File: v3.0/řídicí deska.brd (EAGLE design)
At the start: 119 x 37.2 mm, 26 parts, among them IC1 MC78M12ACDTG, IC2 AZ1117CD5, Q1 NX3008, Q2 NX3008, Q3 NX3008

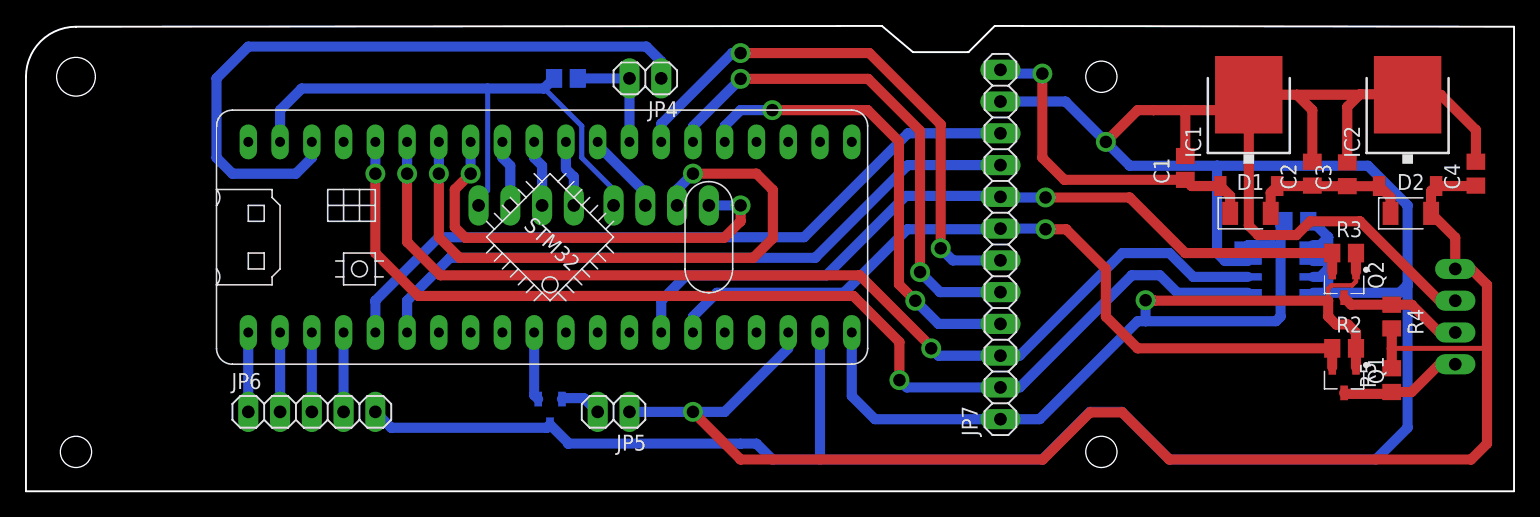
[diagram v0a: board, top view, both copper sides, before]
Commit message: přidána rozlévaná měď, rozšířena dokumentace
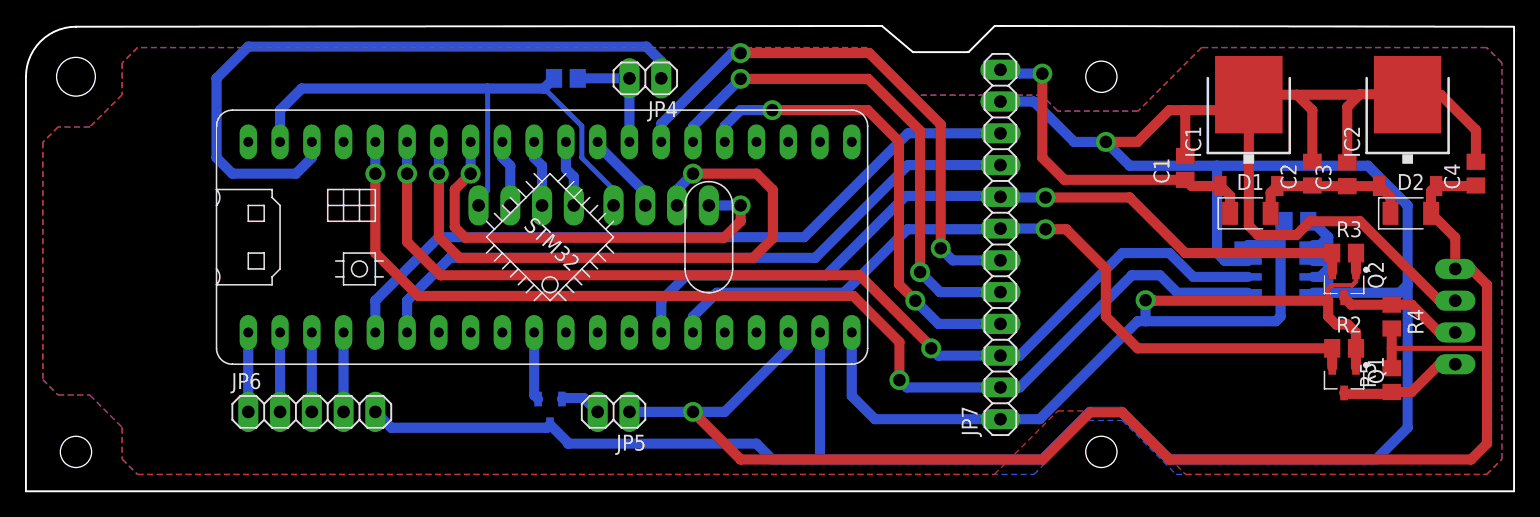
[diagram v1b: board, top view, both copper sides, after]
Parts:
- C1, C2, C3, C4: value 10n -> 100n
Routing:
- added copper zone on layer 1, net GND
- added copper zone on layer 16, net GND
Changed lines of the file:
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@@
 <?xml version="1.0" encoding="utf-8"?>
 <!DOCTYPE eagle SYSTEM "eagle.dtd">
-<eagle version="9.5.1">
+<eagle version="9.7.0">
 <drawing>
 <settings>
@@
 <attribute name="VALUE" x="110.744" y="20.351" size="1.27" layer="27" align="top-center"/>
 </element>
-<element name="C1" library="rcl" library_urn="urn:adsk.eagle:library:334" package="C0805" package3d_urn="urn:adsk.eagle:package:23617/2" value="10n" x="92.71" y="25.8576" smashed="yes" rot="R90">
+<element name="C1" library="rcl" library_urn="urn:adsk.eagle:library:334" package="C0805" package3d_urn="urn:adsk.eagle:package:23617/2" value="100n" x="92.71" y="25.8576" smashed="yes" rot="R90">
 <attribute name="NAME" x="91.44" y="24.5876" size="1.27" layer="25" rot="R90"/>
 <attribute name="POPULARITY" value="88" x="92.71" y="25.8576" size="1.778" layer="27" rot="R90" display="off"/>
@@
 <attribute name="VALUE" x="95.25" y="24.5876" size="1.27" layer="27" rot="R90"/>
 </element>
-<element name="C2" library="rcl" library_urn="urn:adsk.eagle:library:334" package="C0805" package3d_urn="urn:adsk.eagle:package:23617/2" value="10n" x="102.87" y="25.4" smashed="yes" rot="R90">
+<element name="C2" library="rcl" library_urn="urn:adsk.eagle:library:334" package="C0805" package3d_urn="urn:adsk.eagle:package:23617/2" value="100n" x="102.87" y="25.4" smashed="yes" rot="R90">
 <attribute name="NAME" x="101.6" y="24.13" size="1.27" layer="25" rot="R90"/>
 <attribute name="POPULARITY" value="88" x="102.87" y="25.4" size="1.778" layer="27" rot="R90" display="off"/>
@@
 <attribute name="VALUE" x="105.41" y="24.13" size="1.27" layer="27" rot="R90"/>
 </element>
-<element name="C3" library="rcl" library_urn="urn:adsk.eagle:library:334" package="C0805" package3d_urn="urn:adsk.eagle:package:23617/2" value="10n" x="105.664" y="25.3496" smashed="yes" rot="R90">
+<element name="C3" library="rcl" library_urn="urn:adsk.eagle:library:334" package="C0805" package3d_urn="urn:adsk.eagle:package:23617/2" value="100n" x="105.664" y="25.3496" smashed="yes" rot="R90">
 <attribute name="NAME" x="104.394" y="24.0796" size="1.27" layer="25" rot="R90"/>
 <attribute name="POPULARITY" value="88" x="105.664" y="25.3496" size="1.778" layer="27" rot="R90" display="off"/>
@@
 <attribute name="VALUE" x="108.204" y="24.0796" size="1.27" layer="27" rot="R90"/>
 </element>
-<element name="C4" library="rcl" library_urn="urn:adsk.eagle:library:334" package="C0805" package3d_urn="urn:adsk.eagle:package:23617/2" value="10n" x="115.9524" y="25.4" smashed="yes" rot="R90">
+<element name="C4" library="rcl" library_urn="urn:adsk.eagle:library:334" package="C0805" package3d_urn="urn:adsk.eagle:package:23617/2" value="100n" x="115.9524" y="25.4" smashed="yes" rot="R90">
 <attribute name="NAME" x="114.6824" y="24.13" size="1.27" layer="25" rot="R90"/>
 <attribute name="POPULARITY" value="88" x="115.9524" y="25.4" size="1.778" layer="27" rot="R90" display="off"/>
@@
 <wire x1="41.4172" y1="32.2072" x2="42.23" y2="33.02" width="0.8128" layer="16"/>
 <contactref element="Q3" pad="3"/>
-<wire x1="43.35" y1="3.81" x2="57.15" y2="3.81" width="0.8128" layer="16"/>
+<wire x1="43.35" y1="3.81" x2="58.42" y2="3.81" width="0.8128" layer="16"/>
 <wire x1="113.03" y1="15.24" x2="114.3" y2="15.24" width="0.8128" layer="1"/>
 <contactref element="JP6" pad="5"/>
@@
 <wire x1="41.6647" y1="5.08" x2="41.91" y2="5.3253" width="0.8128" layer="16"/>
 <contactref element="JP7" pad="11"/>
-<wire x1="86.36" y1="27.94" x2="83.1342" y2="31.1658" width="0.8128" layer="16"/>
-<wire x1="83.1342" y1="31.1658" x2="77.9282" y2="31.1658" width="0.8128" layer="16"/>
+<wire x1="86.36" y1="27.94" x2="83.82" y2="27.94" width="0.8128" layer="16"/>
+<wire x1="83.82" y1="27.94" x2="80.5942" y2="31.1658" width="0.8128" layer="16"/>
+<wire x1="80.5942" y1="31.1658" x2="77.9282" y2="31.1658" width="0.8128" layer="16"/>
 <via x="86.36" y="27.94" extent="1-16" drill="1"/>
-<wire x1="88.8976" y1="30.4776" x2="90.1676" y2="30.4776" width="0.8128" layer="1"/>
-<wire x1="90.17" y1="30.48" x2="90.1676" y2="30.4776" width="0.8128" layer="1"/>
-<wire x1="90.1676" y1="30.4776" x2="92.71" y2="30.4776" width="0.8128" layer="1"/>
+<wire x1="91.4376" y1="30.4776" x2="92.71" y2="30.4776" width="0.8128" layer="1"/>
 <wire x1="92.71" y1="30.4776" x2="96.5176" y2="30.4776" width="0.8128" layer="1"/>
 <wire x1="96.5176" y1="30.4776" x2="97.79" y2="31.75" width="0.8128" layer="1"/>
@@
 <wire x1="101.64" y1="31.71" x2="106.64" y2="31.71" width="0.8128" layer="1"/>
 <wire x1="106.64" y1="31.71" x2="106.68" y2="31.75" width="0.8128" layer="1"/>
-<wire x1="86.36" y1="27.94" x2="88.8976" y2="30.4776" width="0.8128" layer="1"/>
+<wire x1="91.4376" y1="30.4776" x2="88.9" y2="27.94" width="0.8128" layer="1"/>
+<wire x1="88.9" y1="27.94" x2="86.36" y2="27.94" width="0.8128" layer="1"/>
 <wire x1="102.55" y1="21.59" x2="102.87" y2="21.59" width="0.8128" layer="16"/>
 <wire x1="102.87" y1="21.59" x2="104.14" y2="20.32" width="0.8128" layer="16"/>
@@
 <wire x1="95.885" y1="18.415" x2="95.25" y2="19.05" width="0.8128" layer="16"/>
 <wire x1="95.25" y1="19.05" x2="95.25" y2="26.035" width="0.8128" layer="16"/>
-<wire x1="57.15" y1="3.81" x2="58.42" y2="3.81" width="0.8128" layer="16"/>
 <wire x1="58.42" y1="3.81" x2="59.69" y2="2.54" width="0.8128" layer="16"/>
 <wire x1="59.69" y1="2.54" x2="63.5" y2="2.54" width="0.8128" layer="16"/>
 <wire x1="63.5" y1="12.7" x2="63.5" y2="2.54" width="0.8128" layer="16"/>
-<wire x1="17.78" y1="27.94" x2="20.32" y2="27.94" width="0" layer="19" extent="1-1"/>
-<wire x1="41.91" y1="5.3253" x2="46.99" y2="22.86" width="0" layer="19" extent="16-16"/>
+<polygon width="0.1524" layer="1" spacing="1.27" pour="solid" isolate="0.4064" thermals="yes">
+<vertex x="82.5068375" y="6.4146"/>
+<vertex x="82.53484375" y="6.4262"/>
+<vertex x="87.64515625" y="6.4262"/>
+<vertex x="87.6731625" y="6.4146"/>
+<vertex x="92.7415625" y="1.3462"/>
+<vertex x="116.8084375" y="1.3462"/>
+<vertex x="118.0338" y="2.5715625"/>
+<vertex x="118.0338" y="34.2584375"/>
+<vertex x="116.8084375" y="35.4838"/>
+<vertex x="94.0115625" y="35.4838"/>
+<vertex x="88.9431625" y="30.4154"/>
+<vertex x="88.91515625" y="30.4038"/>
+<vertex x="82.53484375" y="30.4038"/>
+<vertex x="82.5068375" y="30.4154"/>
+<vertex x="81.2484375" y="31.6738"/>
+<vertex x="71.10484375" y="31.6738"/>
+<vertex x="71.0768375" y="31.6854"/>
+<vertex x="67.2784375" y="35.4838"/>
+<vertex x="8.9215625" y="35.4838"/>
+<vertex x="7.6962" y="34.2584375"/>
+<vertex x="7.6962" y="31.73484375"/>
+<vertex x="7.6846" y="31.7068375"/>
+<vertex x="5.1231625" y="29.1454"/>
+<vertex x="5.09515625" y="29.1338"/>
+<vertex x="2.5715625" y="29.1338"/>
+<vertex x="1.3462" y="27.9084375"/>
+<vertex x="1.3462" y="8.9215625"/>
+<vertex x="2.5715625" y="7.6962"/>
+<vertex x="5.09515625" y="7.6962"/>
+<vertex x="5.1231625" y="7.6846"/>
+<vertex x="7.6846" y="5.1231625"/>
+<vertex x="7.6962" y="5.09515625"/>
+<vertex x="7.6962" y="2.5715625"/>
+<vertex x="8.9215625" y="1.3462"/>
+<vertex x="77.4384375" y="1.3462"/>
+</polygon>
+<polygon width="0.1524" layer="16" spacing="1.27" pour="solid" isolate="0.4064" thermals="yes">
+<vertex x="84.9198375" y="5.6526"/>
+<vertex x="84.94784375" y="5.6642"/>
+<vertex x="87.64515625" y="5.6642"/>
+<vertex x="87.6731625" y="5.6526"/>
+<vertex x="91.9795625" y="1.3462"/>
+<vertex x="116.8084375" y="1.3462"/>
+<vertex x="118.0338" y="2.5715625"/>
+<vertex x="118.0338" y="34.2584375"/>
+<vertex x="116.8084375" y="35.4838"/>
+<vertex x="94.0115625" y="35.4838"/>
+<vertex x="88.9431625" y="30.4154"/>
+<vertex x="88.91515625" y="30.4038"/>
+<vertex x="82.53484375" y="30.4038"/>
+<vertex x="82.5068375" y="30.4154"/>
+<vertex x="81.2484375" y="31.6738"/>
+<vertex x="71.10484375" y="31.6738"/>
+<vertex x="71.0768375" y="31.6854"/>
+<vertex x="67.2784375" y="35.4838"/>
+<vertex x="8.9215625" y="35.4838"/>
+<vertex x="7.6962" y="34.2584375"/>
+<vertex x="7.6962" y="31.73484375"/>
+<vertex x="7.6846" y="31.7068375"/>
+<vertex x="5.1231625" y="29.1454"/>
+<vertex x="5.09515625" y="29.1338"/>
+<vertex x="2.5715625" y="29.1338"/>
+<vertex x="1.3462" y="27.9084375"/>
+<vertex x="1.3462" y="8.9215625"/>
+<vertex x="2.5715625" y="7.6962"/>
+<vertex x="5.09515625" y="7.6962"/>
+<vertex x="5.1231625" y="7.6846"/>
+<vertex x="7.6846" y="5.1231625"/>
+<vertex x="7.6962" y="5.09515625"/>
+<vertex x="7.6962" y="2.5715625"/>
+<vertex x="8.9215625" y="1.3462"/>
+<vertex x="80.6134375" y="1.3462"/>
+</polygon>
 </signal>
 <signal name="+3V3">

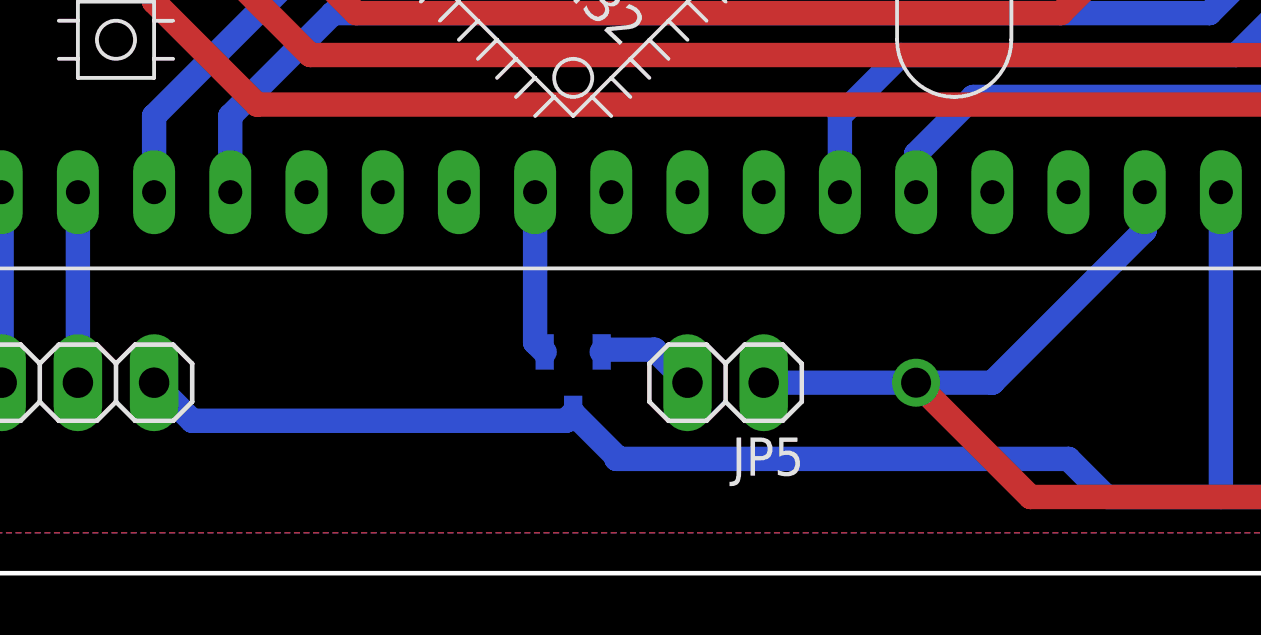
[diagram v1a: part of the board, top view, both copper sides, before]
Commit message: oprava mosfet ventilátoru
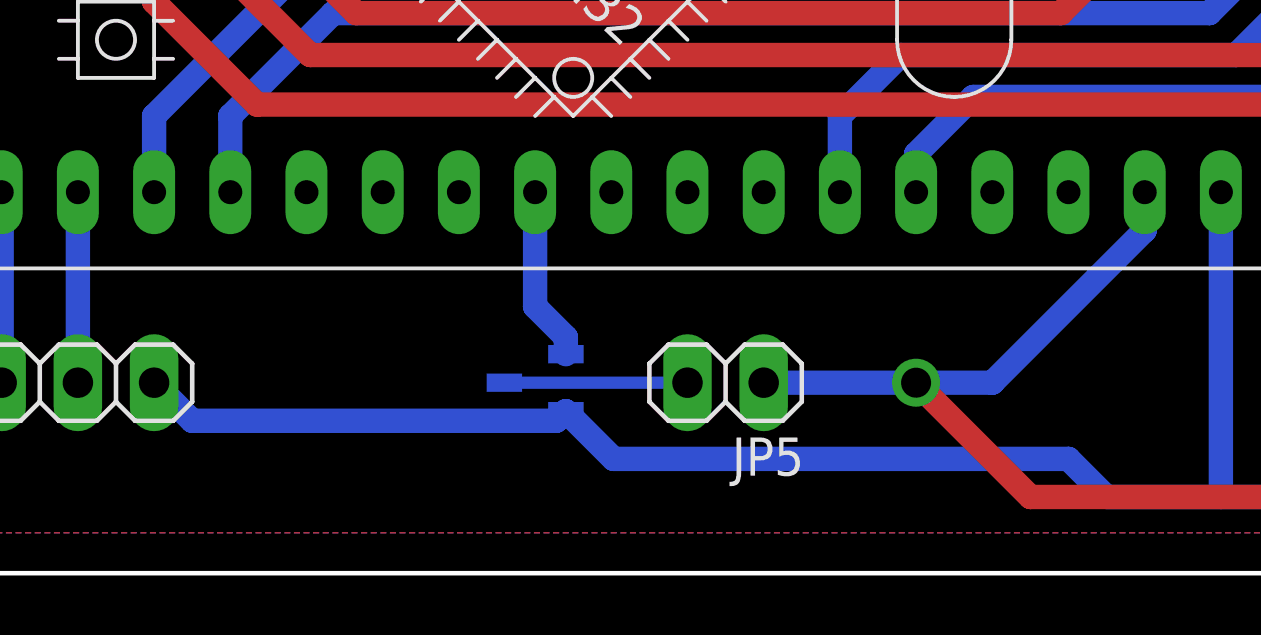
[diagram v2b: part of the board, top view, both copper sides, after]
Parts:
- moved Q3 1.27 mm to (40.6, 6.35), turned to 0 degrees
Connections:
- net GND: now also Q3.2; no longer Q3.3
- net N$5: now also Q3.3; no longer Q3.2
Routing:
- net N$5: track 3.35 -> 6.10 mm
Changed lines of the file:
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@@
 <?xml version="1.0" encoding="utf-8"?>
 <!DOCTYPE eagle SYSTEM "eagle.dtd">
-<eagle version="9.7.0">
+<eagle version="9.5.1">
 <drawing>
 <settings>
@@
 <attribute name="VALUE" x="52.07" y="36.195" size="1.27" layer="27" rot="R180"/>
 </element>
-<element name="Q3" library="NEXPERIA" library_urn="urn:adsk.wipprod:fs.file:vf.nSOLjnv0RT-tOKrwxN9ipw" package="SOT95P240X110-3N" value="NX3008" x="41.91" y="6.35" smashed="yes" rot="MR270">
-<attribute name="NAME" x="40.005" y="8.255" size="1.27" layer="26" rot="MR270"/>
-<attribute name="VALUE" x="45.085" y="8.255" size="1.27" layer="28" rot="MR270"/>
+<element name="Q3" library="NEXPERIA" library_urn="urn:adsk.wipprod:fs.file:vf.nSOLjnv0RT-tOKrwxN9ipw" package="SOT95P240X110-3N" value="NX3008" x="40.64" y="6.35" smashed="yes" rot="MR0">
+<attribute name="NAME" x="42.545" y="8.255" size="1.27" layer="26" rot="MR0"/>
+<attribute name="VALUE" x="42.545" y="3.175" size="1.27" layer="28" rot="MR0"/>
 </element>
 <element name="JP5" library="Connector" package="1X02" package3d_urn="urn:adsk.eagle:package:22435/2" value="PINHD-1X2" x="46.99" y="6.35" smashed="yes" rot="R180">
@@
 <wire x1="36.9196" y1="32.2072" x2="22.0472" y2="32.2072" width="0.8128" layer="16"/>
 <wire x1="41.4172" y1="32.2072" x2="42.23" y2="33.02" width="0.8128" layer="16"/>
-<contactref element="Q3" pad="3"/>
-<wire x1="43.35" y1="3.81" x2="58.42" y2="3.81" width="0.8128" layer="16"/>
 <wire x1="113.03" y1="15.24" x2="114.3" y2="15.24" width="0.8128" layer="1"/>
 <contactref element="JP6" pad="5"/>
 <wire x1="27.94" y1="6.35" x2="29.21" y2="5.08" width="0.8128" layer="16"/>
 <wire x1="97.8388" y1="31.6612" x2="97.79" y2="31.71" width="0.8128" layer="1"/>
-<wire x1="41.91" y1="5.3253" x2="43.35" y2="3.8853" width="0.8128" layer="16"/>
-<wire x1="43.35" y1="3.8853" x2="43.35" y2="3.81" width="0.8128" layer="16"/>
-<wire x1="29.21" y1="5.08" x2="41.6647" y2="5.08" width="0.8128" layer="16"/>
-<wire x1="41.6647" y1="5.08" x2="41.91" y2="5.3253" width="0.8128" layer="16"/>
 <contactref element="JP7" pad="11"/>
 <wire x1="86.36" y1="27.94" x2="83.82" y2="27.94" width="0.8128" layer="16"/>
@@
 <wire x1="59.69" y1="2.54" x2="63.5" y2="2.54" width="0.8128" layer="16"/>
 <wire x1="63.5" y1="12.7" x2="63.5" y2="2.54" width="0.8128" layer="16"/>
-<polygon width="0.1524" layer="1" spacing="1.27" pour="solid" isolate="0.4064" thermals="yes">
+<polygon width="0.1524" layer="1" isolate="0.4064">
 <vertex x="82.5068375" y="6.4146"/>
 <vertex x="82.53484375" y="6.4262"/>
@@
 <vertex x="77.4384375" y="1.3462"/>
 </polygon>
-<polygon width="0.1524" layer="16" spacing="1.27" pour="solid" isolate="0.4064" thermals="yes">
+<polygon width="0.1524" layer="16" isolate="0.4064">
 <vertex x="84.9198375" y="5.6526"/>
 <vertex x="84.94784375" y="5.6642"/>
@@
 <vertex x="80.6134375" y="1.3462"/>
 </polygon>
+<contactref element="Q3" pad="2"/>
+<wire x1="29.21" y1="5.08" x2="41.3447" y2="5.08" width="0.8128" layer="16"/>
+<wire x1="41.3447" y1="5.08" x2="41.6647" y2="5.4" width="0.8128" layer="16"/>
+<wire x1="41.6647" y1="5.4" x2="43.2547" y2="3.81" width="0.8128" layer="16"/>
+<wire x1="43.2547" y1="3.81" x2="58.42" y2="3.81" width="0.8128" layer="16"/>
+<wire x1="17.78" y1="27.94" x2="20.32" y2="27.94" width="0" layer="19" extent="1-1"/>
+<wire x1="41.6647" y1="5.4" x2="46.99" y2="22.86" width="0" layer="19" extent="16-16"/>
 </signal>
 <signal name="+3V3">
@@
 <signal name="PA15">
 <contactref element="U$1" pad="P$10"/>
-<wire x1="40.64" y1="12.7" x2="40.64" y2="7.6947" width="0.8128" layer="16"/>
 <contactref element="Q3" pad="1"/>
-<wire x1="40.64" y1="7.6947" x2="40.96" y2="7.3747" width="0.8128" layer="16"/>
+<wire x1="41.6647" y1="7.3" x2="41.6647" y2="7.8653" width="0.8128" layer="16"/>
+<wire x1="41.6647" y1="7.8653" x2="40.64" y2="8.89" width="0.8128" layer="16"/>
+<wire x1="40.64" y1="8.89" x2="40.64" y2="12.7" width="0.8128" layer="16"/>
 </signal>
 <signal name="N$5">
-<contactref element="Q3" pad="2"/>
 <contactref element="JP5" pad="2"/>
-<wire x1="45.72" y1="6.35" x2="44.62" y2="7.45" width="0.8128" layer="16"/>
-<wire x1="44.62" y1="7.45" x2="42.9353" y2="7.45" width="0.8128" layer="16"/>
-<wire x1="42.9353" y1="7.45" x2="42.86" y2="7.3747" width="0.8128" layer="16"/>
+<contactref element="Q3" pad="3"/>
+<wire x1="39.6153" y1="6.35" x2="45.72" y2="6.35" width="0.4064" layer="16"/>
 </signal>
 <signal name="N$6">
